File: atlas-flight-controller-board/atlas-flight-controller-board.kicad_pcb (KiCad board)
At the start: 4 copper layers, 38 parts, among them IC1 LSM6DSV80XTR, IC2 LPS22HHTR, J2 Ultimate GPS Breakout Socket, J4 5V Input Power, U1 LIS2MDL, U2 DEV-16771

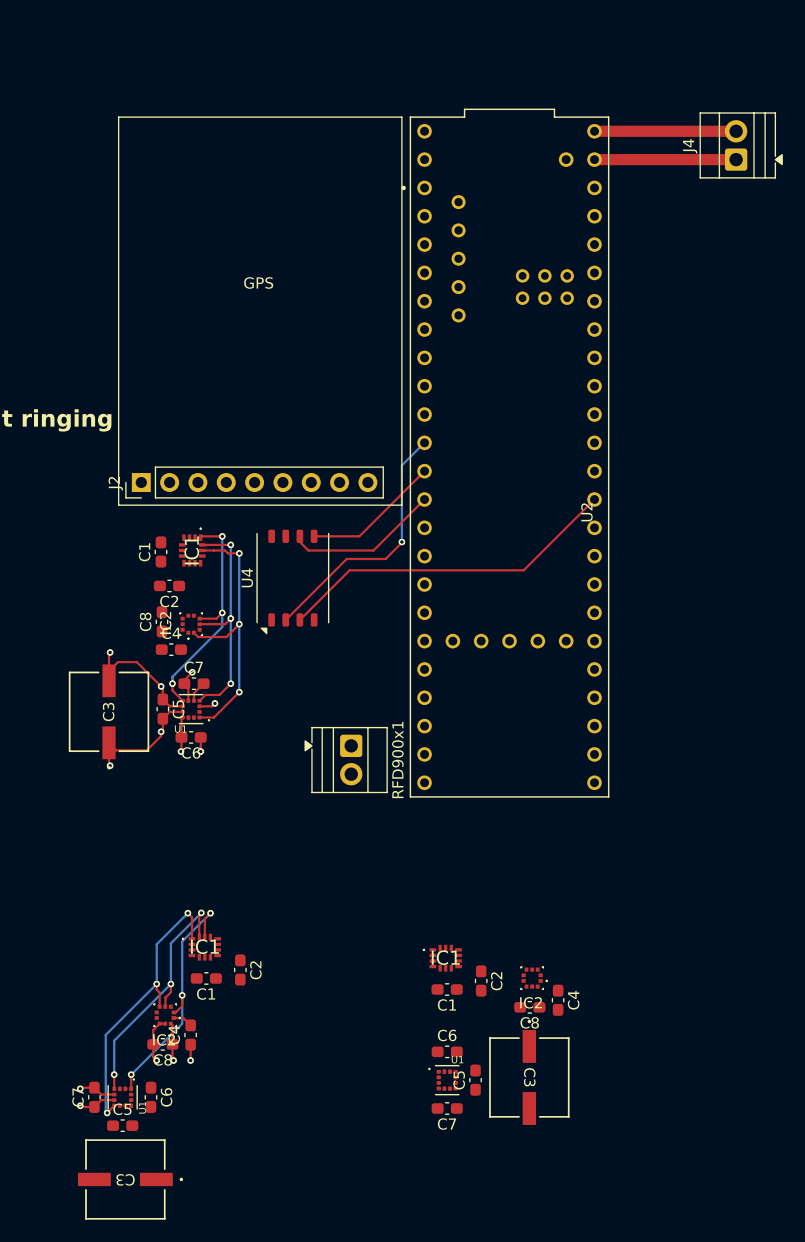
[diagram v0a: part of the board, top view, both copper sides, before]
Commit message: Sensor and Flash layout finished besides MISO, MOSI resistors (reduce ringing). Added plated M2 mounting holes.
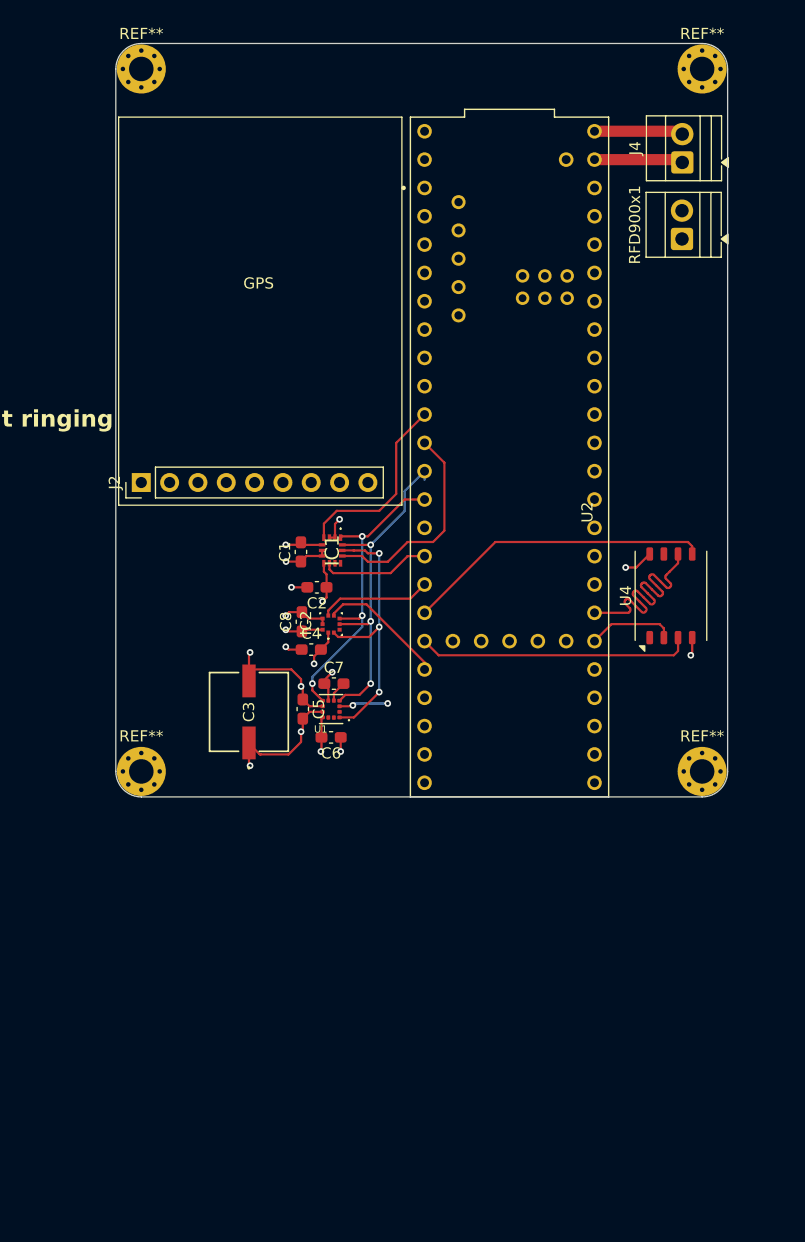
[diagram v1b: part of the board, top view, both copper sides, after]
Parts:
- removed the C1 at (101.1, 133.1)
- removed the C1 at (122.7, 134.1)
- removed the C2 at (125.7, 133.3)
- removed the C2 at (104.1, 132.4)
- removed the C3 at (130.0, 142.0)
- removed the C3 at (93.8, 151.1)
- removed the C3 at (92.4, 109.2)
- removed the C4 at (99.7, 138.2)
- removed the C4 at (132.6, 135.1)
- removed the C5 at (93.6, 146.3)
- removed the C5 at (125.2, 142.2)
- removed the C6 at (96.1, 143.8)
- removed the C6 at (122.7, 139.7)
- removed the C7 at (91.0, 143.8)
- removed the C7 at (122.7, 144.8)
- removed the C8 at (130.1, 135.7)
- removed the C8 at (97.2, 139.0)
- removed the IC1 at (122.5, 131.3)
- removed the IC1 at (100.9, 130.3)
- removed the IC2 at (97.4, 136.4)
- removed the IC2 at (130.3, 133.1)
- removed the U1 at (93.6, 143.8)
- removed the U1 at (122.7, 142.2)
- added C3: 10 uF, APA0606100M050R:CAP_APA_0606_AVX, F.Cu at (104.9, 109.2)
- added REF**: MountingHole_2.2mm_M2_Pad_Via, MountingHole:MountingHole_2.2mm_M2_Pad_Via, F.Cu at (95.2, 51.6)
- added REF**: MountingHole_2.2mm_M2_Pad_Via, MountingHole:MountingHole_2.2mm_M2_Pad_Via, F.Cu at (95.2, 114.6)
- added REF**: MountingHole_2.2mm_M2_Pad_Via, MountingHole:MountingHole_2.2mm_M2_Pad_Via, F.Cu at (145.5, 51.6)
- added REF**: MountingHole_2.2mm_M2_Pad_Via, MountingHole:MountingHole_2.2mm_M2_Pad_Via, F.Cu at (145.5, 114.6)
- moved RFD900x1 54.3 mm to (143.7, 66.8), turned to 90 degrees
- moved U4 33.9 mm to (142.7, 98.8)
- moved C2 13.2 mm to (111.0, 98.0)
- moved C4 12.5 mm to (110.5, 103.6)
- moved C5 12.5 mm to (109.7, 109.0)
- moved C7 12.5 mm to (112.5, 106.7)
- moved IC2 12.5 mm to (112.3, 101.3)
- moved C1 12.5 mm to (109.6, 94.9)
- moved C6 12.5 mm to (112.3, 111.5)
- moved C8 12.5 mm to (109.7, 101.1)
- moved IC1 12.5 mm to (112.4, 94.7)
- moved U1 12.5 mm to (112.3, 109.0)
- moved J4 4.83 mm to (143.8, 59.9)
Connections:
- IC1 pad 1: MISO_1 -> MISO_MEMS
- IC1 pad 13: SCK_1 -> SCK_MEMS
- IC1 pad 14: MOSI_1 -> MOSI_MEMS
- IC2 pad 2: SCK_1 -> SCK_MEMS
- IC2 pad 4: MOSI_1 -> MOSI_MEMS
- IC2 pad 5: MISO_1 -> MISO_MEMS
- U1 pad 1: SCK_1 -> SCK_MEMS
- U1 pad 4: MOSI_1 -> MOSI_MEMS
- U1 pad 7: MISO_1 -> MISO_MEMS
- U2 pad 10: CS_SD -> CS_IMU
- U2 pad 11: MOSI -> MOSI_MEMS
- U2 pad 12: MISO -> MISO_MEMS
- U2 pad 13: SCK -> SCK_MEMS
- U2 pad 20: unconnected-(U2-A6-Pad20) -> UART_MCU_TX_RFD900_RX
- U2 pad 21: unconnected-(U2-A7-Pad21) -> UART_RFD900_TX_MCU_RX
- U2 pad 24: UART_MCU_TX_RFD900_RX -> IMU_INT2
- U2 pad 25: UART_RFD900_TX_MCU_RX -> BARO_INT
- U2 pad 26: MOSI_1 -> MOSI_SD
- U2 pad 27: SCK_1 -> SCK_SD
- U2 pad 28: unconnected-(U2-RX7-Pad28) -> CS_BARO
- U2 pad 29: unconnected-(U2-TX7-Pad29) -> CS_MAG
- U2 pad 33: BARO_INT -> unconnected-(U2-MCLK2-Pad33)
- U2 pad 34: IMU_INT2 -> unconnected-(U2-RX8-Pad34)
- U2 pad 35: IMU_INT1 -> unconnected-(U2-TX8-Pad35)
- U2 pad 36: CS_IMU -> unconnected-(U2-CS2-Pad36)
- U2 pad 37: CS_BARO -> unconnected-(U2-CS3-Pad37)
- U2 pad 38: CS_MAG -> CS_SD
- U2 pad 39: MISO_1 -> MISO_SD
- U2 pad 9: unconnected-(U2-OUT1C-Pad9) -> IMU_INT1
- U4 pad 3: SCK -> SCK_SD
- U4 pad 5: MOSI -> MOSI_SD
- U4 pad 6: MISO -> MISO_SD
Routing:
- net SCK_1: track 48.2 -> 0.00 mm, vias 6 -> 0
- net MISO_1: track 47.9 -> 0.00 mm, vias 6 -> 0
- net MOSI_1: track 45.0 -> 0.00 mm, vias 6 -> 0
- net SCK: track 30.9 -> 0.00 mm
- net MOSI_MEMS: track 0.00 -> 30.8 mm, vias 0 -> 3
- net MISO_MEMS: track 0.00 -> 28.2 mm, vias 0 -> 3
- net MOSI_SD: track 0.00 -> 27.5 mm
- net SCK_MEMS: track 0.00 -> 25.0 mm, vias 0 -> 3
- net MISO_SD: track 0.00 -> 24.7 mm
- net SCK_SD: track 0.00 -> 24.6 mm
- net CS_IMU: track 0.00 -> 19.1 mm
- net IMU_INT1: track 0.00 -> 17.0 mm
- net CS_SD: track 23.1 -> 7.84 mm, vias 1 -> 0
- net MISO: track 13.9 -> 0.00 mm
- net +3V3: track 19.6 -> 32.3 mm, vias 4 -> 8
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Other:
- board outline added: 54.9 x 67.6 mm

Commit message: Fixing a couple things here and there. Need to add LEDs still and route external LEDs
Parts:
- added J1: LED Indicator Header, TerminalBlock:TerminalBlock_Xinya_XY308-2.54-2P_1x02_P2.54mm_Horizontal, F.Cu at (145.0, 67.8)
- added R1: 10, Resistor_SMD:R_0603_1608Metric_Pad0.98x0.95mm_HandSolder, F.Cu at (140.5, 68.3)
- added R2: 10, Resistor_SMD:R_0603_1608Metric_Pad0.98x0.95mm_HandSolder, F.Cu at (140.5, 64.8)
- moved RFD900x1 8.73 mm to (145.0, 75.4)
- moved J4 1.24 mm to (145.0, 59.9)
- moved REF** 0.76 mm to (146.3, 51.6)
- moved REF** 0.76 mm to (146.3, 114.6)
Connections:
- U2 pad 22: unconnected-(U2-A8-Pad22) -> L_led
- U2 pad 23: unconnected-(U2-A9-Pad23) -> R_led
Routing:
- net UART_GPS_TX_MCU_RX: track 0.00 -> 35.3 mm
- net UART_MCU_TX_GPS_RX: track 0.00 -> 31.7 mm
- net GPS_FIX: track 0.00 -> 31.2 mm
- net SCK_MEMS: track 25.0 -> 46.3 mm
- net GND: track 39.8 -> 43.8 mm, vias 10 -> 11
- net CS_MAG: track 4.42 -> 7.94 mm, vias 2 -> 1
- net +3V3: track 32.3 -> 35.1 mm, vias 8 -> 9
- net +5V: track 7.98 -> 9.22 mm
- net MOSI_MEMS: track 30.8 -> 30.0 mm
- net CS_IMU: track 19.1 -> 18.6 mm, vias 0 -> 2
- added copper zone on In2.Cu, net +3V3
- added copper zone on In1.Cu, net GND
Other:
- board size 54.9 x 67.6 mm -> 55.6 x 67.6 mm
- board text added: "Need: - LEDS - Labeling where applicable - Ground traces?"
- board text added: "{dblquote}Twenty years from now you will be more disappointed by the things that you didn't do than by the ones you did do. So throw off the bowlines. Sail away from the safe harbor. Catch the trade winds in your sails. Explore. Dream. Discover.{dblquote}"
- board text removed: "NEED Resistors on MISO MOSI to figure out ringing"

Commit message: Done.
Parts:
- removed J2: Ultimate GPS Breakout Socket, Connector_PinHeader_2.54mm:PinHeader_1x09_P2.54mm_Vertical
- removed U4: ~, ZDSD16GLGIAG:LGA-8_8x6.2mm_P1.27mm
- added D1: APHBM2012LSURKZGKC, APHBM2012LSURKZGKC:LED_APHBM2012LSURKZGKC, F.Cu at (141.7, 84.1)
- added D2: APHBM2012LSURKZGKC, APHBM2012LSURKZGKC:LED_APHBM2012LSURKZGKC, F.Cu at (141.7, 91.2)
- added D3: APHBM2012LSURKZGKC, APHBM2012LSURKZGKC:LED_APHBM2012LSURKZGKC, F.Cu at (141.7, 87.6)
- added D4: APHBM2012LSURKZGKC, APHBM2012LSURKZGKC:LED_APHBM2012LSURKZGKC, F.Cu at (141.7, 106.6)
- added R10: 100, Resistor_SMD:R_0603_1608Metric_Pad0.98x0.95mm_HandSolder, F.Cu at (145.5, 107.4)
- added R3: 100, Resistor_SMD:R_0603_1608Metric_Pad0.98x0.95mm_HandSolder, F.Cu at (145.5, 83.3)
- added R4: 100, Resistor_SMD:R_0603_1608Metric_Pad0.98x0.95mm_HandSolder, F.Cu at (145.5, 84.9)
- added R5: 100, Resistor_SMD:R_0603_1608Metric_Pad0.98x0.95mm_HandSolder, F.Cu at (145.5, 90.5)
- added R6: 100, Resistor_SMD:R_0603_1608Metric_Pad0.98x0.95mm_HandSolder, F.Cu at (145.5, 92.0)
- added R7: 100, Resistor_SMD:R_0603_1608Metric_Pad0.98x0.95mm_HandSolder, F.Cu at (145.5, 86.9)
- added R8: 100, Resistor_SMD:R_0603_1608Metric_Pad0.98x0.95mm_HandSolder, F.Cu at (145.5, 88.4)
- added R9: 100, Resistor_SMD:R_0603_1608Metric_Pad0.98x0.95mm_HandSolder, F.Cu at (145.5, 105.9)
- added SrvCtr1: Servo Ctrl, TerminalBlock:TerminalBlock_Xinya_XY308-2.54-2P_1x02_P2.54mm_Horizontal, F.Cu at (145.0, 79.8)
- added U3: 746, 746:XCVR_746, F.Cu at (106.0, 73.7)
- added U5: ~, ZDSD16GLGIAG:LGA-8_8x6.2mm_P1.27mm, F.Cu at (142.8, 99.0)
- moved RFD900x1 2.29 mm to (145.0, 73.2)
- moved J1 1.27 mm to (145.0, 66.5)
- moved R1 1.27 mm to (140.5, 67.1), turned to 90 degrees
- moved R2 1.27 mm to (140.5, 63.5)
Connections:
- U2 pad 14: unconnected-(U2-A0-Pad14) -> USER_1_Green
- U2 pad 15: unconnected-(U2-A1-Pad15) -> USER_2_Green
- U2 pad 16: unconnected-(U2-A2-Pad16) -> Ping_Red
- U2 pad 17: unconnected-(U2-A3-Pad17) -> Ping_Green
- U2 pad 18: unconnected-(U2-A4-Pad18) -> Servo_1
- U2 pad 19: unconnected-(U2-A5-Pad19) -> Servo_2
- U2 pad 36: unconnected-(U2-CS2-Pad36) -> SD_LED_Red
- U2 pad 37: unconnected-(U2-CS3-Pad37) -> SD_LED_Green
- U2 pad 6: unconnected-(U2-OUT1D-Pad6) -> USER_2_Red
- U2 pad 8: unconnected-(U2-TX2-Pad8) -> USER_1_Red
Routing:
- net USER_2_Red: track 0.00 -> 25.7 mm
- net USER_1_Red: track 0.00 -> 25.0 mm
- net GND: track 43.8 -> 54.9 mm, vias 11 -> 15
- net Servo_1: track 0.00 -> 10.3 mm
- net Servo_2: track 0.00 -> 10.1 mm
- net UART_MCU_TX_RFD900_RX: track 0.00 -> 9.97 mm
- net UART_RFD900_TX_MCU_RX: track 0.00 -> 9.46 mm
- net Ping_Green: track 0.00 -> 6.44 mm
- net USER_1_Green: track 0.00 -> 6.23 mm
- net USER_2_Green: track 0.00 -> 5.80 mm
- net Ping_Red: track 0.00 -> 5.78 mm
- net R_led: track 0.00 -> 5.48 mm
- net SD_LED_Red: track 0.00 -> 5.28 mm
- net SD_LED_Green: track 0.00 -> 5.25 mm
- net L_led: track 0.00 -> 4.84 mm
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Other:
- board text added: "Clr/Empty"
- board text added: "Ping"
- board text added: "Usr1"
- board text added: "Usr2"
- board text removed: "Need: - LEDS - Labeling where applicable - Ground traces?"

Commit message: Fab files via external tooling
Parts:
- renumbered RFD900x1 to Radio's
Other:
- board text added: "Put me back!"
- board text added: "Rx Tx"
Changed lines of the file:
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@@
 		(tenting front back)
 		(pcbplotparams
-			(layerselection 0x00000000_00000000_55555555_5755f5ff)
+			(layerselection 0x00000000_00000000_5555555f_5755f5ff)
 			(plot_on_all_layers_selection 0x00000000_00000000_00000000_00000000)
 			(disableapertmacros no)
@@
 			(outputformat 1)
 			(mirror no)
-			(drillshape 1)
+			(drillshape 0)
 			(scaleselection 1)
 			(outputdirectory "")
@@
 			(at 1.27 -2.286 90)
 			(layer "F.SilkS")
+			(hide yes)
 			(effects
 				(font
@@
 			(at 1.27 -3.22 90)
 			(layer "F.SilkS")
+			(hide yes)
 			(effects
 				(font
@@
 			(at 0 -3.15 0)
 			(layer "F.SilkS")
+			(hide yes)
 			(effects
 				(font
@@
 			(at 0 -3.15 0)
 			(layer "F.SilkS")
+			(hide yes)
 			(effects
 				(font
@@
 			(at 0 -3.15 0)
 			(layer "F.SilkS")
+			(hide yes)
 			(effects
 				(font
@@
 			(at 0 -3.15 0)
 			(layer "F.SilkS")
+			(hide yes)
 			(effects
 				(font
@@
 		(at 106 73.66)
 		(property "Reference" "U3"
-			(at -9.775 -19.03 0)
+			(at -10.16 -1.27 0)
 			(layer "F.SilkS")
+			(hide yes)
 			(effects
 				(font
@@
 		(descr "Terminal Block Xinya XY308-2.54-2P, 2 pins, pitch 2.54mm, size 5.58x6.5mm, drill diameter 1.2mm, pad diameter 2mm, http://www.xinyaelectronic.com/product/xy308-254, script-generated using https://gitlab.com/kicad/libraries/kicad-footprint-generator/-/tree/master/scripts/TerminalBlock_Xinya")
 		(tags "THT Terminal Block Xinya XY308-2.54-2P pitch 2.54mm size 5.58x6.5mm drill 1.2mm pad 2mm")
-		(property "Reference" "RFD900x1"
-			(at 1.27 -4.318 90)
+		(property "Reference" "Radio's"
+			(at 0.762 -5.334 90)
 			(layer "F.SilkS")
 			(effects
@@
 		(layer "Edge.Cuts")
 	)
+	(gr_text "Put me back!"
+		(at 128.905 91.694 90)
+		(layer "F.SilkS")
+		(effects
+			(font
+				(size 1 1)
+				(thickness 0.1)
+			)
+			(justify left bottom)
+		)
+	)
+	(gr_text "Rx Tx"
+		(at 141.605 74.295 90)
+		(layer "F.SilkS")
+		(effects
+			(font
+				(size 1 1)
+				(thickness 0.1)
+			)
+			(justify left bottom)
+		)
+	)
 	(gr_text "Usr1"
